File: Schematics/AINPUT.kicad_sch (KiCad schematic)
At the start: 28 parts, among them J2 AudioJack2_Switch, J3 AudioJack2_Switch, U2 Opamp_Dual

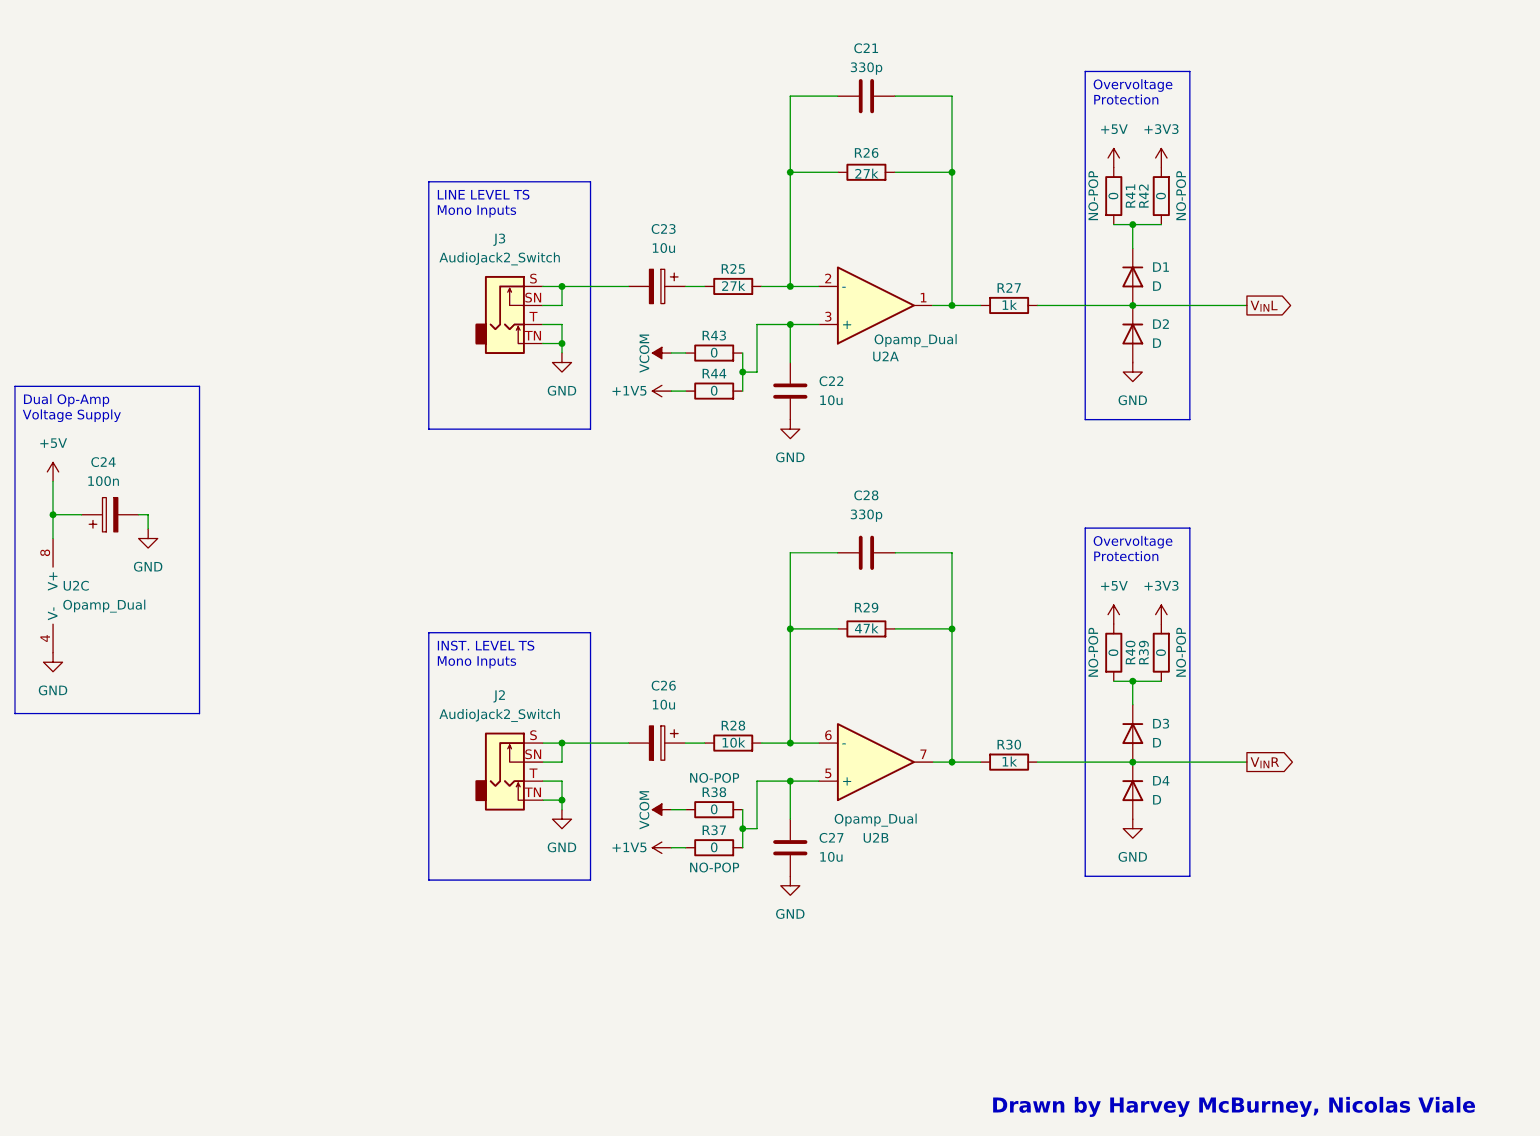
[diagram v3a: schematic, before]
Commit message: Started adding footprints, changed values.
Added footprints for most components. need to check in uni which sizes are available and what will need to be ordered from mouser.
Changed line in/out to TRS as this will be more reliable and added 0 ohm resistor options to bypass mono input and use line in/out as stereo.
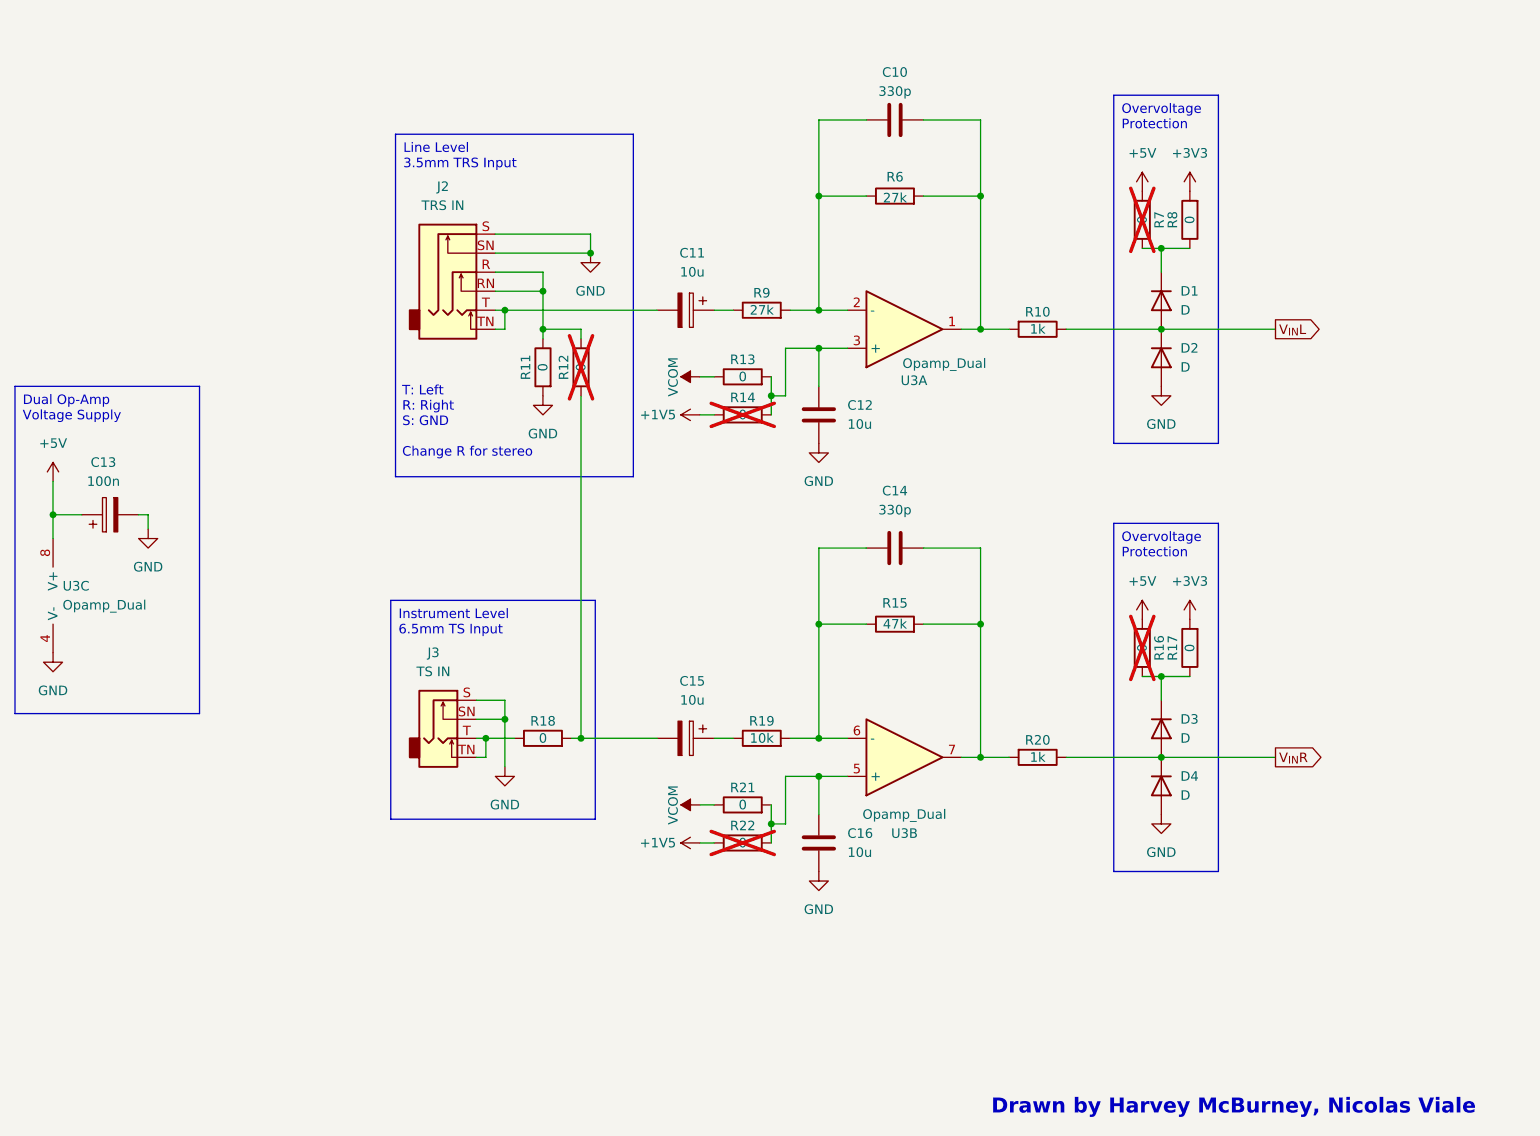
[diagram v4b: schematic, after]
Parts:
- removed J3: AudioJack2_Switch, symbol Connector_Audio:AudioJack2_Switch
- added J2: TRS IN, symbol Connector_Audio:AudioJack3_Switch
- added R11, R12, R18: 0, Resistor_SMD:R_0603_1608Metric_Pad0.98x0.95mm_HandSolder, symbol Device:R
- J3: renamed from J2; value AudioJack2_Switch -> TS IN; footprint (none) -> Connector_Audio:Jack_6.35mm_Neutrik_NMJ4HHD2_Horizontal
- R10: renamed from R27; footprint (none) -> Resistor_SMD:R_0603_1608Metric_Pad0.98x0.95mm_HandSolder
- R13: renamed from R43; footprint (none) -> Resistor_SMD:R_0603_1608Metric_Pad0.98x0.95mm_HandSolder
- R14: renamed from R44; footprint (none) -> Resistor_SMD:R_0603_1608Metric_Pad0.98x0.95mm_HandSolder; now not fitted
- R15: renamed from R29; footprint (none) -> Resistor_SMD:R_0603_1608Metric_Pad0.98x0.95mm_HandSolder
- R16: renamed from R40; footprint (none) -> Resistor_SMD:R_0603_1608Metric_Pad0.98x0.95mm_HandSolder; pop NO-POP -> (none); now not fitted
- R17: renamed from R39; footprint (none) -> Resistor_SMD:R_0603_1608Metric_Pad0.98x0.95mm_HandSolder; pop NO-POP -> (none)
- R19: renamed from R28; footprint (none) -> Resistor_SMD:R_0603_1608Metric_Pad0.98x0.95mm_HandSolder
- R20: renamed from R30; footprint (none) -> Resistor_SMD:R_0603_1608Metric_Pad0.98x0.95mm_HandSolder
- R21: renamed from R38; footprint (none) -> Resistor_SMD:R_0603_1608Metric_Pad0.98x0.95mm_HandSolder; pop NO-POP -> (none)
- R22: renamed from R37; footprint (none) -> Resistor_SMD:R_0603_1608Metric_Pad0.98x0.95mm_HandSolder; pop NO-POP -> (none); now not fitted
- R6: renamed from R26; footprint (none) -> Resistor_SMD:R_0603_1608Metric_Pad0.98x0.95mm_HandSolder
- R7: renamed from R41; footprint (none) -> Resistor_SMD:R_0603_1608Metric_Pad0.98x0.95mm_HandSolder; pop NO-POP -> (none); now not fitted
- R8: renamed from R42; footprint (none) -> Resistor_SMD:R_0603_1608Metric_Pad0.98x0.95mm_HandSolder; pop NO-POP -> (none)
- R9: renamed from R25; footprint (none) -> Resistor_SMD:R_0603_1608Metric_Pad0.98x0.95mm_HandSolder
- renumbered C21 to C10, C23 to C11, C22 to C12, C24 to C13, C28 to C14, C26 to C15, C27 to C16, U2 to U3
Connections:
- net GND: now also J3.S, J3.SN, J2.S, J2.SN, R11.2; no longer J3.T, J3.TN
- net at C11.2: now also J2.T, J2.TN
- new net: C15.2, R12.2, R18.2
- new net: J2.R, J2.RN, R11.1, R12.1
- new net: J3.T, J3.TN, R18.1
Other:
- note added: "T: Left R: Right S: GND Change R for stereo"
- moved on the sheet: C10, C11, C12, C14, C15, C16, D1, D2, D3, D4, J3, R10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

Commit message: Updated to KiCAD v9
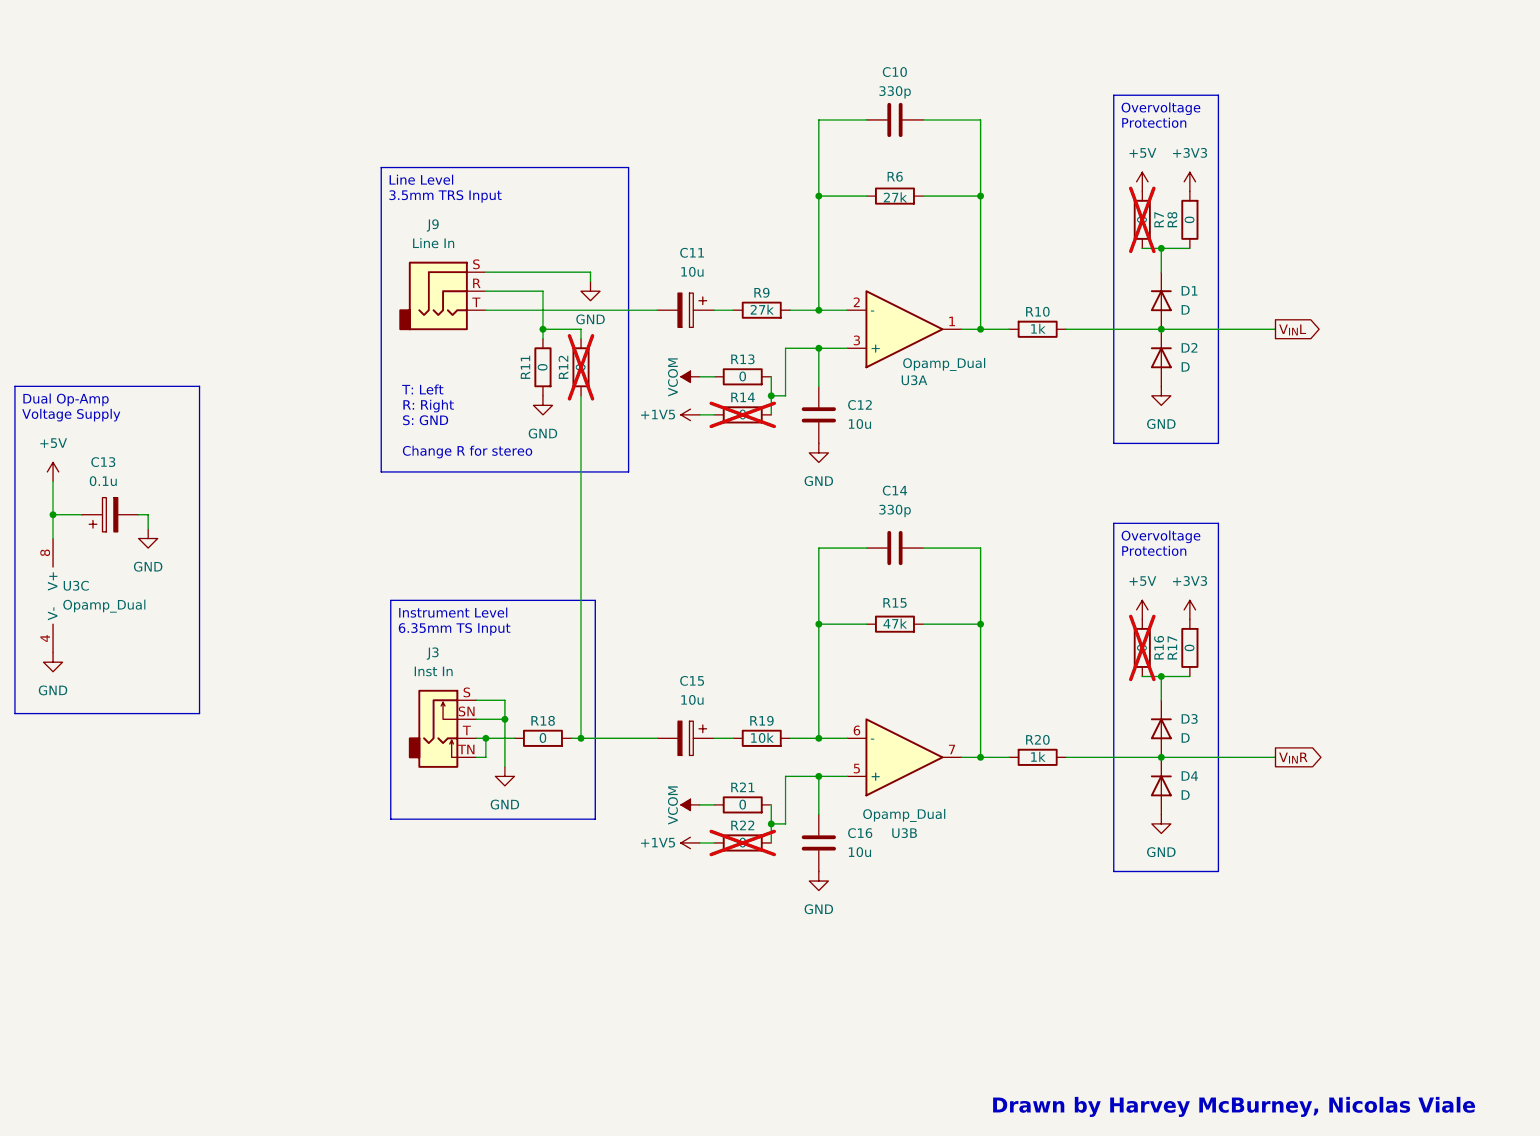
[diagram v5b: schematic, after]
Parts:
- removed J2: TRS IN, symbol Connector_Audio:AudioJack3_Switch
- added J9: Line In, Connector_Audio:Jack_3.5mm_CUI_SJ1-3523N_Horizontal, symbol Connector_Audio:AudioJack3
- C11, C12, C15, C16: footprint (none) -> Capacitor_SMD:CP_Elec_5x5.4
- C13: value 100n -> 0.1u
- J3: value TS IN -> Inst In
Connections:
- net GND: now also J9.S
- net at C11.2: now also J9.T
- net at R11.1, R12.1: now also J9.R

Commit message: Added all footprints, updated PCB
Added footprints using uni available components where possible. Might be necessary to change op-amps as they are large and not made for audio. PCB has a mockup of component placements but probably needs expanded.
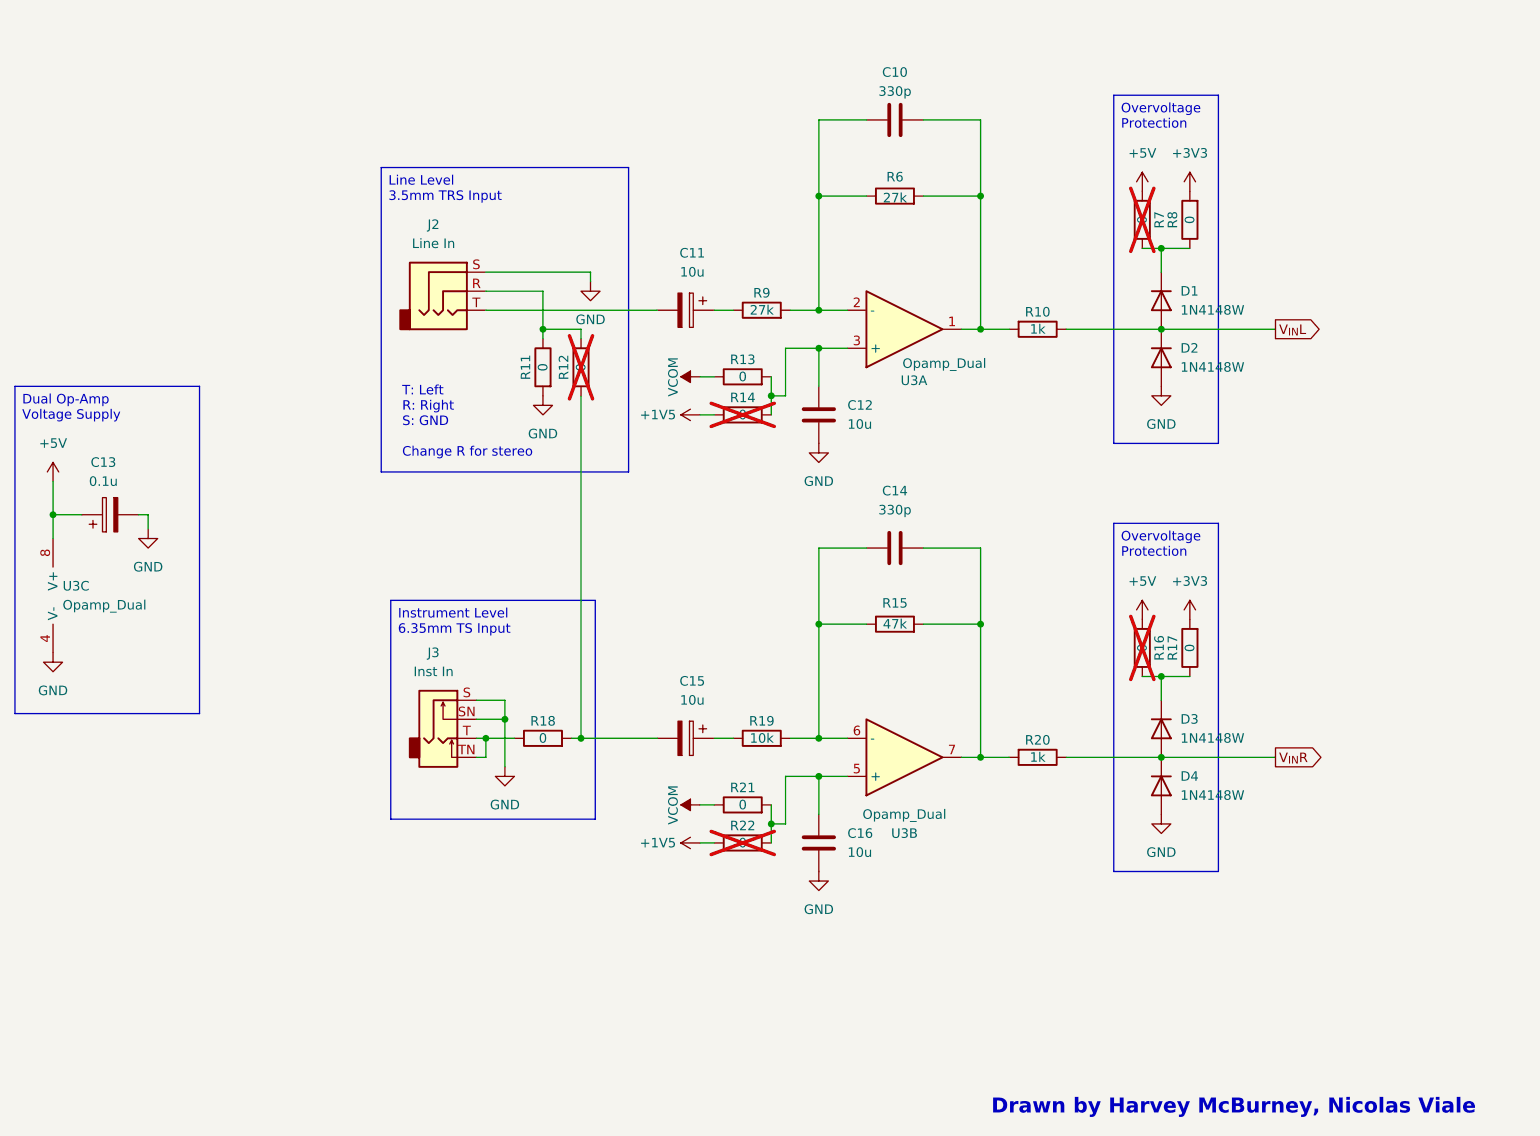
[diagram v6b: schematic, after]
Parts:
- removed D1, D2, D3, D4: D, symbol Device:D
- added D1, D2, D3, D4: 1N4148W, Diode_SMD:D_SOD-123, symbol Diode:1N4148W
- C10, C13, C14: footprint (none) -> Capacitor_SMD:C_0805_2012Metric_Pad1.18x1.45mm_HandSolder
- R10, R11, R12, R13, R14, R15, R16, R17, R18, R19, R20, R21, R22, R6, R7, R8, R9: footprint Resistor_SMD:R_0603_1608Metric_Pad0.98x0.95mm_HandSolder -> Resistor_SMD:R_0805_2012Metric_Pad1.20x1.40mm_HandSolder
- U3: footprint (none) -> Package_DIP:DIP-8_W7.62mm_Socket
- renumbered J9 to J2
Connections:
- net GND: now also D2.2 (A), D4.2 (A)
- net V_{IN}L: now also D1.2 (A), D2.1 (K)
- net V_{IN}R: now also D3.2 (A), D4.1 (K)
- net at R7.2, R8.1: now also D1.1 (K)
- net at R16.2, R17.1: now also D3.1 (K)

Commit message: Adjusted Capacitor Footprints
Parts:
- C11, C12, C15, C16: footprint Capacitor_SMD:CP_Elec_5x5.4 -> Capacitor_SMD:CP_Elec_4x5.7
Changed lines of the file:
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@@
 			)
 		)
-		(property "Footprint" "Capacitor_SMD:CP_Elec_5x5.4"
+		(property "Footprint" "Capacitor_SMD:CP_Elec_4x5.7"
 			(at 133.35 64.4652 0)
 			(effects
@@
 			)
 		)
-		(property "Footprint" "Capacitor_SMD:CP_Elec_5x5.4"
+		(property "Footprint" "Capacitor_SMD:CP_Elec_4x5.7"
 			(at 133.35 121.6152 0)
 			(effects
@@
 			)
 		)
-		(property "Footprint" "Capacitor_SMD:CP_Elec_5x5.4"
+		(property "Footprint" "Capacitor_SMD:CP_Elec_4x5.7"
 			(at 155.9052 138.43 0)
 			(effects
@@
 			)
 		)
-		(property "Footprint" "Capacitor_SMD:CP_Elec_5x5.4"
+		(property "Footprint" "Capacitor_SMD:CP_Elec_4x5.7"
 			(at 155.9052 81.28 0)
 			(effects

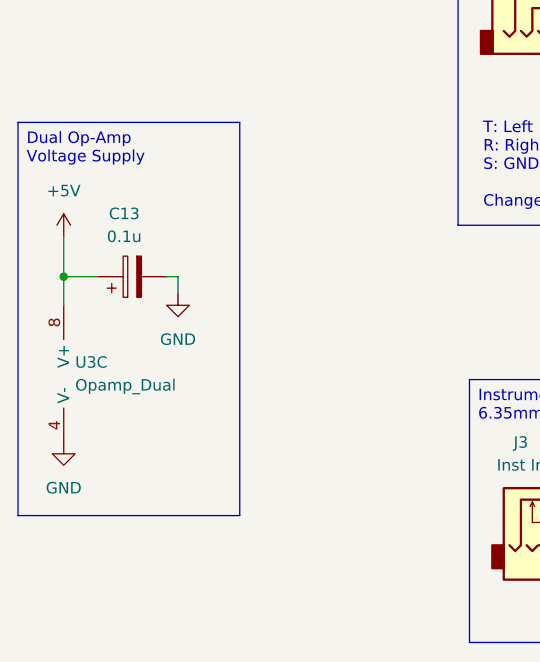
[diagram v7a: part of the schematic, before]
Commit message: Changed footprints, added 3d model to GPIO
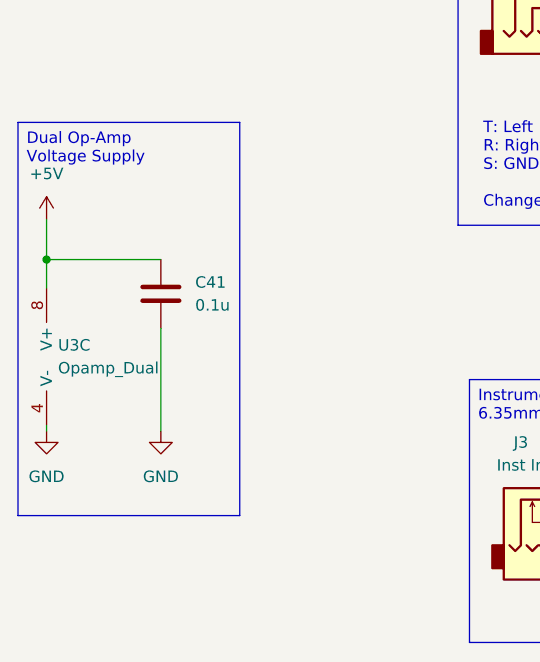
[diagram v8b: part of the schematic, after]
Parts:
- removed C13: 0.1u, Capacitor_SMD:C_0805_2012Metric_Pad1.18x1.45mm_HandSolder, symbol Device:C_Polarized
- added C41: 0.1u, Capacitor_SMD:C_0805_2012Metric_Pad1.18x1.45mm_HandSolder, symbol Device:C
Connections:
- net +5V: now also C41.1
- net GND: now also C41.2
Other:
- moved on the sheet: U3C
